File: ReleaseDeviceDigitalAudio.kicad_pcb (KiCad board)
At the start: 4 copper layers, 132 x 68.5 mm, 179 parts, among them J1 Conn_02x08_Counter_Clockwise, J2 ATMEGA_PROG, J3 SignalStrength, J4 UIBoardCON1, J5 Conn_01x04, J6 UIBoardCON2, J7 KeySwitch, Q1 BSS314PEH6327XTSA1, Q3 SQ2362ES-T1_GE3, Q4 SQD50P06-15L_GE3, U1 ATmega4809-A, U10 ULN2003F12FN-7, U11 ULN2003F12FN-7, U12 ULN2003F12FN-7, U13 ULN2003F12FN-7, U14 MAX98089ETN+, U15 SN74LV1T126, U16 SN74LV1T126, U17 BM83SM1-00TA, U18 PCF85063A, U2 VOMA617A, U3 VOMA617A, U4 LM53635LQRNL*Q1, U5 TLVH431AQDBVRQ1, U6 LM74610-Q1, U7 Compute_Module_4_Connectors, U8 CD4514BM, U9 CD4511BPWR, Y1 9HT12

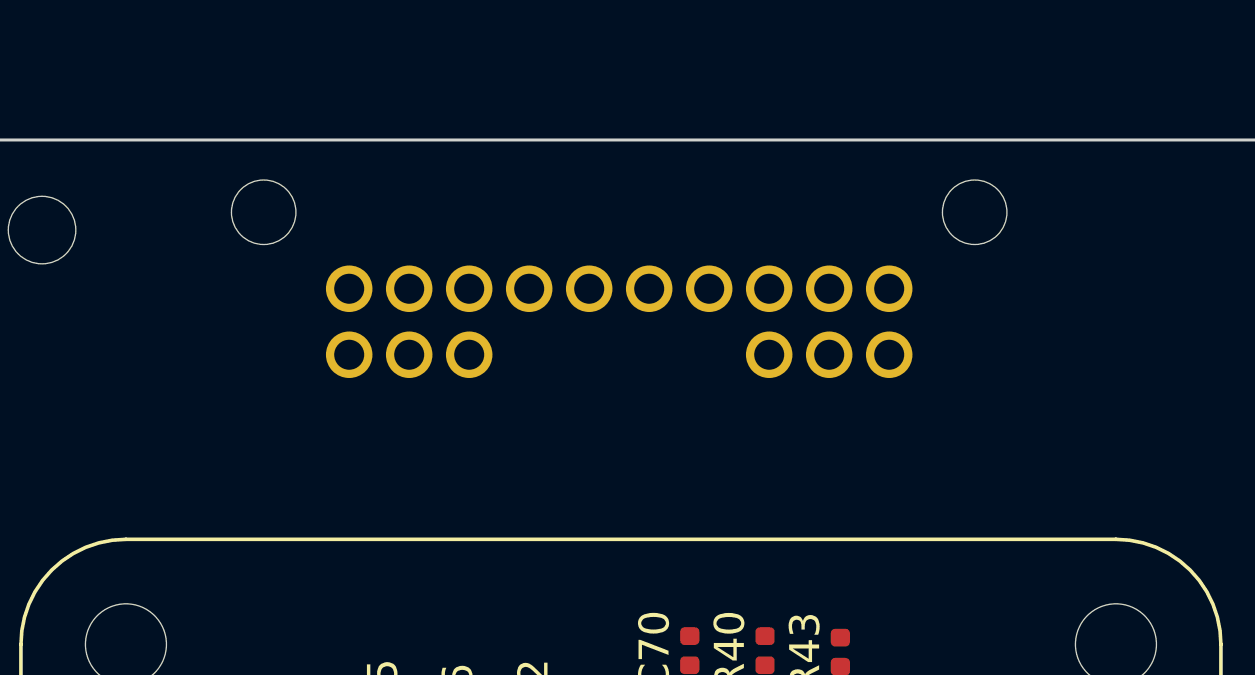
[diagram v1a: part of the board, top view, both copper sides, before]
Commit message: - auf 20pol Audiostecker umgebaut
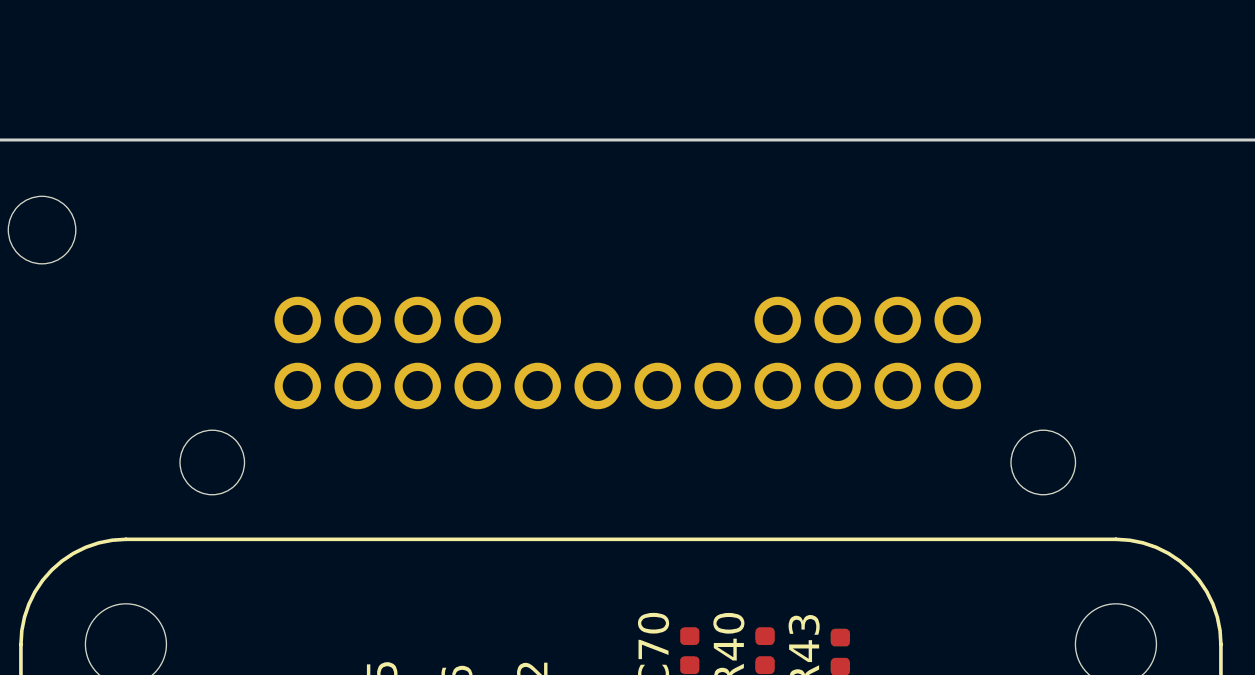
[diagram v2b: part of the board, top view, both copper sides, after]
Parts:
- J1: value Conn_02x08_Counter_Clockwise -> Conn_02x10_Counter_Clockwise; footprint TeKaDe:Molex_34825-0160 -> TeKaDe:Molex_34825-0200
- moved J1 20.3 mm to (173.5, 67.0), turned to 180 degrees
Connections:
- J1 pad 1: /Audio_Master_Out_L -> GND
- J1 pad 10: GND -> /Audio_Master_Out_L
- J1 pad 11: /HeadsetMicInN -> /Line_In_R
- J1 pad 12: /HeadsetMicInP -> /Line_In_L
- J1 pad 14: /Line_In_R -> /Audio_Handset_Out_L
- J1 pad 15: GND -> /Audio_Handset_Out_R
- J1 pad 16: /MasterMicInN -> GND
- J1 pad 3: /Audio_Handset_Out_L -> GND
- J1 pad 4: /Line_In_L -> GND
- J1 pad 6: /MasterMicInP -> GND
- J1 pad 7: /Audio_Master_Out_R -> GND
- J1 pad 9: /Audio_Handset_Out_R -> /Audio_Master_Out_R
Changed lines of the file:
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@@
     (add_net GND)
+  )
+  (module TeKaDe:Molex_34825-0200 (layer B.Cu)
+    (at 173.5 67 180)
+    (descr "Through hole straight socket strip, 2x10, 2.00mm pitch, double cols (from Kicad 4.0.7), script generated")
+    (tags "Through hole socket strip THT 2x10 2.00mm double row")
+    (fp_text reference J1 (at -6 0 270) (layer B.SilkS)
+      (effects (font (size 1 1) (thickness 0.15)) (justify mirror))
+    )
+    (fp_text value Conn_02x10_Counter_Clockwise (at 11 -5 180) (layer B.Fab)
+      (effects (font (size 1 1) (thickness 0.15)) (justify mirror))
+    )
+    (fp_text user %R (at 9 -1 180) (layer B.Fab)
+      (effects (font (size 1 1) (thickness 0.15)) (justify mirror))
+    )
+    (fp_line (start 27 -7) (end -5 -7) (layer B.CrtYd) (width 0.05))
+    (fp_line (start 27 6) (end 27 -7) (layer B.CrtYd) (width 0.05))
+    (fp_line (start -5 6) (end 27 6) (layer B.CrtYd) (width 0.05))
+    (fp_line (start -5 -7) (end -5 6) (layer B.CrtYd) (width 0.05))
+    (fp_line (start -5 4.94) (end -5 6) (layer B.SilkS) (width 0.12))
+    (fp_line (start -5 6) (end -3.94 6) (layer B.SilkS) (width 0.12))
+    (fp_line (start -5 4) (end -3 4) (layer B.SilkS) (width 0.12))
+    (fp_line (start -3 4) (end -3 6) (layer B.SilkS) (width 0.12))
+    (fp_line (start -3 6) (end 27 6) (layer B.SilkS) (width 0.12))
+    (fp_line (start 27 -7) (end 27 6) (layer B.SilkS) (width 0.12))
+    (fp_line (start -5 -7) (end 27 -7) (layer B.SilkS) (width 0.12))
+    (fp_line (start -5 -7) (end -5 4) (layer B.SilkS) (width 0.12))
+    (fp_line (start 23 -3) (end -1 -3) (layer B.Fab) (width 0.1))
+    (fp_line (start 23 1) (end 23 -3) (layer B.Fab) (width 0.1))
+    (fp_line (start 0 1) (end 23 1) (layer B.Fab) (width 0.1))
+    (fp_line (start -1 0) (end 0 1) (layer B.Fab) (width 0.1))
+    (fp_line (start -1 -3) (end -1 0) (layer B.Fab) (width 0.1))
+    (pad 20 thru_hole oval (at 22 -2.2 90) (size 1.55 1.55) (drill 1) (layers *.Cu *.Mask)
+      (net 15 /HeadsetMicInP))
+    (pad 19 thru_hole oval (at 20 -2.2 90) (size 1.55 1.55) (drill 1) (layers *.Cu *.Mask)
+      (net 10 /HeadsetMicInN))
+    (pad 18 thru_hole oval (at 18 -2.2 90) (size 1.55 1.55) (drill 1) (layers *.Cu *.Mask)
+      (net 13 /MasterMicInP))
+    (pad 17 thru_hole oval (at 16 -2.2 90) (size 1.55 1.55) (drill 1) (layers *.Cu *.Mask)
+      (net 8 /MasterMicInN))
+    (pad "" np_thru_hole circle (at 24.85 -4.75 180) (size 2.15 2.15) (drill 2.15) (layers *.Cu *.Mask))
+    (pad "" np_thru_hole circle (at -2.85 -4.75 180) (size 2.15 2.15) (drill 2.15) (layers *.Cu *.Mask))
+    (pad 7 thru_hole oval (at 20 0 90) (size 1.55 1.55) (drill 1) (layers *.Cu *.Mask)
+      (net 2 GND))
+    (pad 8 thru_hole oval (at 22 0 90) (size 1.55 1.55) (drill 1) (layers *.Cu *.Mask)
+      (net 2 GND))
+    (pad 9 thru_hole oval (at 0 -2.2 90) (size 1.55 1.55) (drill 1) (layers *.Cu *.Mask)
+      (net 17 /Audio_Master_Out_R))
+    (pad 10 thru_hole oval (at 2 -2.2 90) (size 1.55 1.55) (drill 1) (layers *.Cu *.Mask)
+      (net 12 /Audio_Master_Out_L))
+    (pad 11 thru_hole oval (at 4 -2.2 90) (size 1.55 1.55) (drill 1) (layers *.Cu *.Mask)
+      (net 21 /Line_In_R))
+    (pad 12 thru_hole oval (at 6 -2.2 90) (size 1.55 1.55) (drill 1) (layers *.Cu *.Mask)
+      (net 22 /Line_In_L))
+    (pad 13 thru_hole oval (at 8 -2.2 90) (size 1.55 1.55) (drill 1) (layers *.Cu *.Mask)
+      (net 2 GND))
+    (pad 14 thru_hole oval (at 10 -2.2 90) (size 1.55 1.55) (drill 1) (layers *.Cu *.Mask)
+      (net 19 /Audio_Handset_Out_L))
+    (pad 15 thru_hole oval (at 12 -2.2 90) (size 1.55 1.55) (drill 1) (layers *.Cu *.Mask)
+      (net 20 /Audio_Handset_Out_R))
+    (pad 16 thru_hole oval (at 14 -2.2 90) (size 1.55 1.55) (drill 1) (layers *.Cu *.Mask)
+      (net 2 GND))
+    (pad 6 thru_hole oval (at 18 0 90) (size 1.55 1.55) (drill 1) (layers *.Cu *.Mask)
+      (net 2 GND))
+    (pad 5 thru_hole oval (at 16 0 90) (size 1.55 1.55) (drill 1) (layers *.Cu *.Mask)
+      (net 2 GND))
+    (pad 4 thru_hole oval (at 6 0 90) (size 1.55 1.55) (drill 1) (layers *.Cu *.Mask)
+      (net 2 GND))
+    (pad 3 thru_hole oval (at 4 0 90) (size 1.55 1.55) (drill 1) (layers *.Cu *.Mask)
+      (net 2 GND))
+    (pad 1 thru_hole oval (at 0 0 90) (size 1.55 1.55) (drill 1) (layers *.Cu *.Mask)
+      (net 2 GND))
+    (pad 2 thru_hole oval (at 2 0 90) (size 1.55 1.55) (drill 1) (layers *.Cu *.Mask)
+      (net 2 GND))
+    (model ${KIPRJMOD}/libs/348250200.stp
+      (offset (xyz 11 -0.5 5.8))
+      (scale (xyz 1 1 1))
+      (rotate (xyz 0 0 0))
+    )
   )
   (module TeKaDe:BM83SM1 (layer F.Cu)
@@
     )
   )
-  (module TeKaDe:Molex_34825-0160 (layer B.Cu)
-    (at 153.215 68.159)
-    (descr "Through hole straight socket strip, 2x10, 2.00mm pitch, double cols (from Kicad 4.0.7), script generated")
-    (tags "Through hole socket strip THT 2x10 2.00mm double row")
-    (fp_text reference J1 (at -6 0 -90) (layer B.SilkS)
-      (effects (font (size 1 1) (thickness 0.15)) (justify mirror))
-    )
-    (fp_text value Conn_02x08_Counter_Clockwise (at 9 -5 180) (layer B.Fab)
-      (effects (font (size 1 1) (thickness 0.15)) (justify mirror))
-    )
-    (fp_text user %R (at 9 -1 180) (layer B.Fab)
-      (effects (font (size 1 1) (thickness 0.15)) (justify mirror))
-    )
-    (fp_line (start 23 -7) (end -5 -7) (layer B.CrtYd) (width 0.05))
-    (fp_line (start 23 6) (end 23 -7) (layer B.CrtYd) (width 0.05))
-    (fp_line (start -5 6) (end 23 6) (layer B.CrtYd) (width 0.05))
-    (fp_line (start -5 -7) (end -5 6) (layer B.CrtYd) (width 0.05))
-    (fp_line (start -5 4.94) (end -5 6) (layer B.SilkS) (width 0.12))
-    (fp_line (start -5 6) (end -3.94 6) (layer B.SilkS) (width 0.12))
-    (fp_line (start -5 4) (end -3 4) (layer B.SilkS) (width 0.12))
-    (fp_line (start -3 4) (end -3 6) (layer B.SilkS) (width 0.12))
-    (fp_line (start -3 6) (end 23 6) (layer B.SilkS) (width 0.12))
-    (fp_line (start 23 -7) (end 23 6) (layer B.SilkS) (width 0.12))
-    (fp_line (start -5 -7) (end 23 -7) (layer B.SilkS) (width 0.12))
-    (fp_line (start -5 -7) (end -5 4) (layer B.SilkS) (width 0.12))
-    (fp_line (start 19 -3) (end -1 -3) (layer B.Fab) (width 0.1))
-    (fp_line (start 19 1) (end 19 -3) (layer B.Fab) (width 0.1))
-    (fp_line (start 0 1) (end 19 1) (layer B.Fab) (width 0.1))
-    (fp_line (start -1 0) (end 0 1) (layer B.Fab) (width 0.1))
-    (fp_line (start -1 -3) (end -1 0) (layer B.Fab) (width 0.1))
-    (pad "" np_thru_hole circle (at 20.85 -4.75) (size 2.15 2.15) (drill 2.15) (layers *.Cu *.Mask))
-    (pad "" np_thru_hole circle (at -2.85 -4.75) (size 2.15 2.15) (drill 2.15) (layers *.Cu *.Mask))
-    (pad 7 thru_hole oval (at 0 -2.2 270) (size 1.55 1.55) (drill 1) (layers *.Cu *.Mask)
-      (net 17 /Audio_Master_Out_R))
-    (pad 8 thru_hole oval (at 2 -2.2 270) (size 1.55 1.55) (drill 1) (layers *.Cu *.Mask)
-      (net 2 GND))
-    (pad 9 thru_hole oval (at 4 -2.2 270) (size 1.55 1.55) (drill 1) (layers *.Cu *.Mask)
-      (net 20 /Audio_Handset_Out_R))
-    (pad 10 thru_hole oval (at 6 -2.2 270) (size 1.55 1.55) (drill 1) (layers *.Cu *.Mask)
-      (net 2 GND))
-    (pad 11 thru_hole oval (at 8 -2.2 270) (size 1.55 1.55) (drill 1) (layers *.Cu *.Mask)
-      (net 10 /HeadsetMicInN))
-    (pad 12 thru_hole oval (at 10 -2.2 270) (size 1.55 1.55) (drill 1) (layers *.Cu *.Mask)
-      (net 15 /HeadsetMicInP))
-    (pad 13 thru_hole oval (at 12 -2.2 270) (size 1.55 1.55) (drill 1) (layers *.Cu *.Mask)
-      (net 2 GND))
-    (pad 14 thru_hole oval (at 14 -2.2 270) (size 1.55 1.55) (drill 1) (layers *.Cu *.Mask)
-      (net 21 /Line_In_R))
-    (pad 15 thru_hole oval (at 16 -2.2 270) (size 1.55 1.55) (drill 1) (layers *.Cu *.Mask)
-      (net 2 GND))
-    (pad 16 thru_hole oval (at 18 -2.2 270) (size 1.55 1.55) (drill 1) (layers *.Cu *.Mask)
-      (net 8 /MasterMicInN))
-    (pad 6 thru_hole oval (at 18 0 270) (size 1.55 1.55) (drill 1) (layers *.Cu *.Mask)
-      (net 13 /MasterMicInP))
-    (pad 5 thru_hole oval (at 16 0 270) (size 1.55 1.55) (drill 1) (layers *.Cu *.Mask)
-      (net 2 GND))
-    (pad 4 thru_hole oval (at 14 0 270) (size 1.55 1.55) (drill 1) (layers *.Cu *.Mask)
-      (net 22 /Line_In_L))
-    (pad 3 thru_hole oval (at 4 0 270) (size 1.55 1.55) (drill 1) (layers *.Cu *.Mask)
-      (net 19 /Audio_Handset_Out_L))
-    (pad 1 thru_hole oval (at 0 0 270) (size 1.55 1.55) (drill 1) (layers *.Cu *.Mask)
-      (net 12 /Audio_Master_Out_L))
-    (pad 2 thru_hole oval (at 2 0 270) (size 1.55 1.55) (drill 1) (layers *.Cu *.Mask)
-      (net 2 GND))
-    (model ${KIPRJMOD}/libs/348250160.stp
-      (offset (xyz 9 -0.5 5.8))
-      (scale (xyz 1 1 1))
-      (rotate (xyz 0 0 0))
-    )
-  )
